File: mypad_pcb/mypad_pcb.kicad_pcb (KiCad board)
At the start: 2 copper layers, 76.2 x 96 mm, 59 parts, among them J1 USB_C_Receptacle_USB2.0, SW1 SW_BOOTMODE, SW10 +, SW11 4, SW12 5, SW13 6, SW14 1, SW15 2, SW16 3, SW17 0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

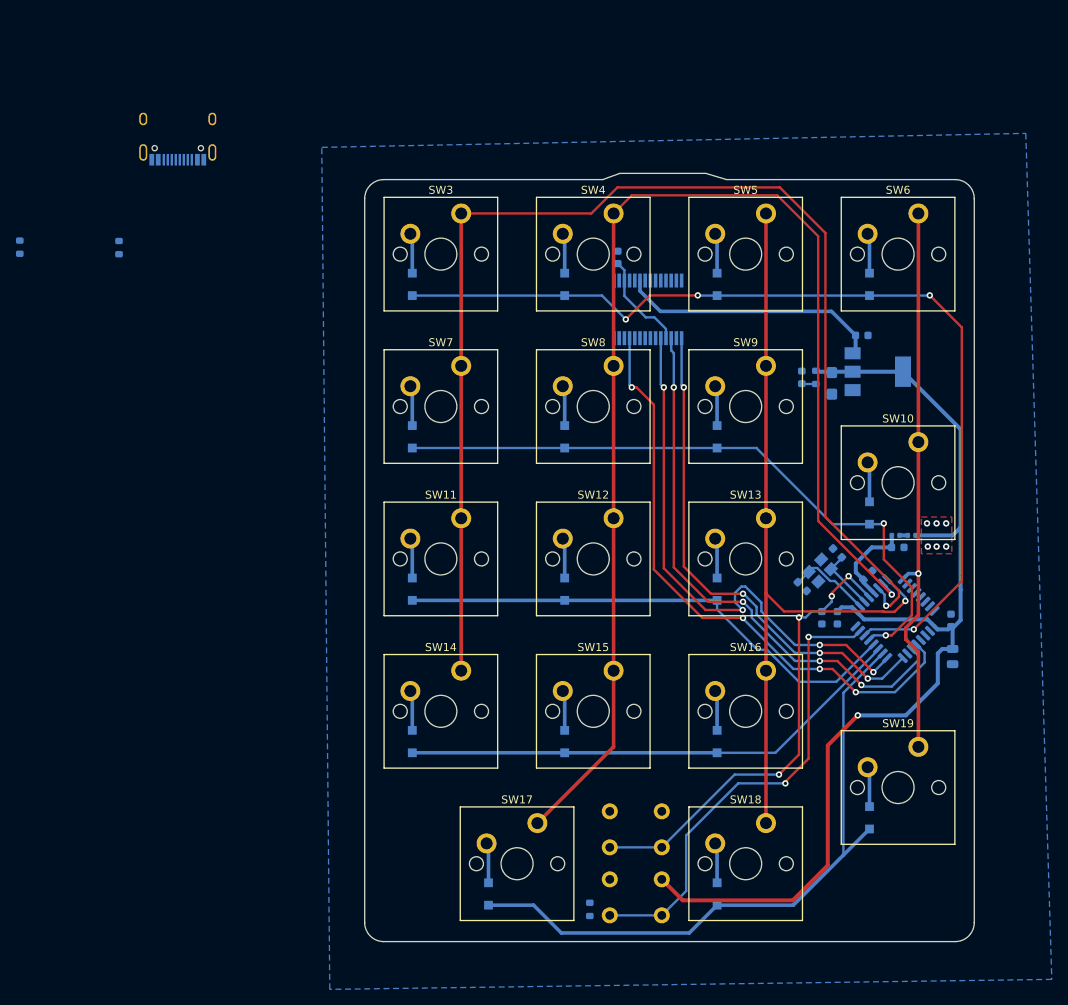
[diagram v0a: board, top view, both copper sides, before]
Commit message: Swap components for STM32F042C6 compatible ones
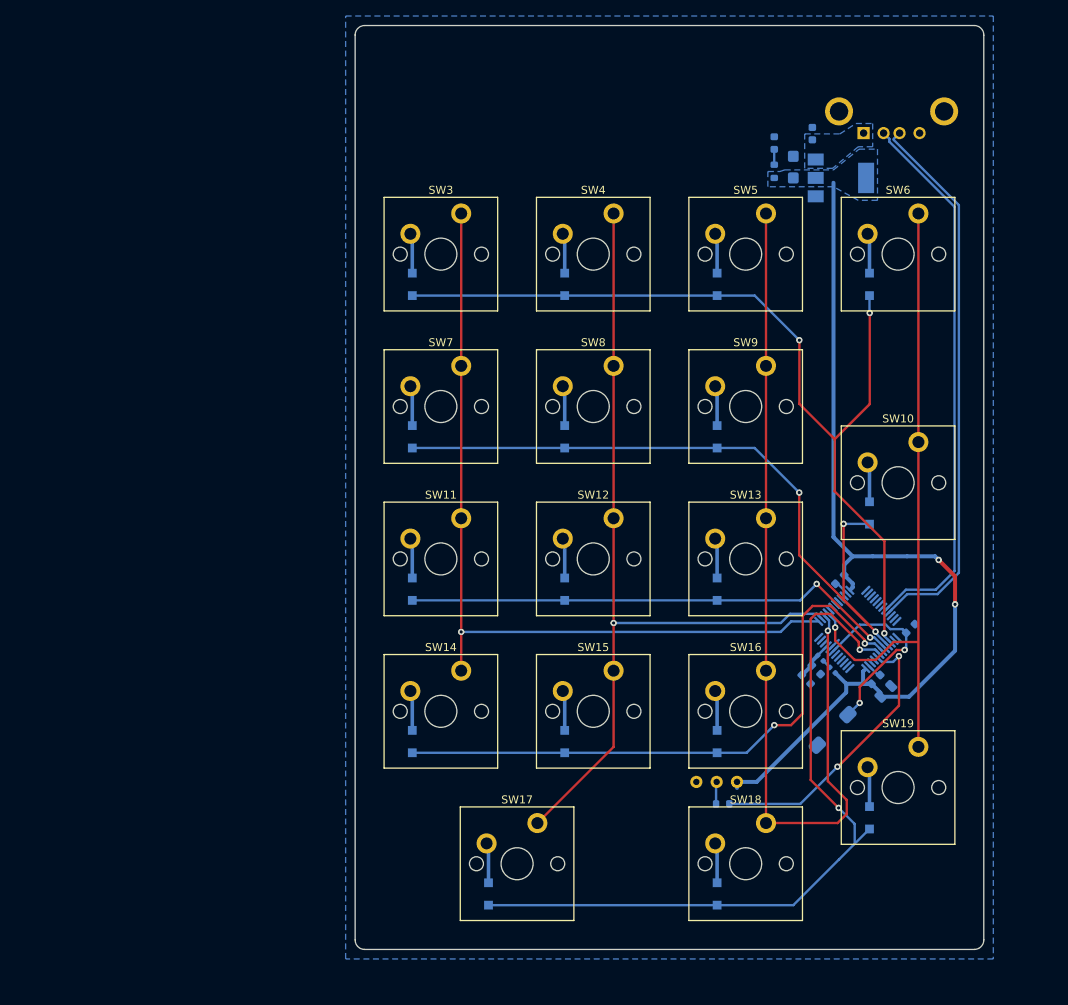
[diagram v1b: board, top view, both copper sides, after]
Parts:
- removed C1: 100n, Capacitor_SMD:C_0603_1608Metric
- removed C10, C11: 12p, Capacitor_SMD:C_0603_1608Metric
- removed R1, R2: 5k1, Resistor_SMD:R_0603_1608Metric
- removed U3: STM32F030K6Tx, Package_QFP:LQFP-32_7x7mm_P0.8mm
- removed Y1: 16MHz, Crystal:Crystal_SMD_3225-4Pin_3.2x2.5mm
- C9: value 0u1 -> 100n
- J1: value USB_C_Receptacle_USB2.0 -> USB_A; footprint Connector_USB:USB_C_Receptacle_HRO_TYPE-C-31-M-12 -> Connector_USB:USB_A_CONNFLY_DS1095-WNR0
- SW1: value SW_BOOTMODE -> SW_SPDT; footprint Button_Switch_THT:SW_PUSH_6mm -> Button_Switch_THT:ESP_SPDT_Slide_Switch
- SW2: footprint Button_Switch_THT:SW_PUSH_6mm -> Button_Switch_SMD:DTSM31N_SMD_Tact_Switch_4.3mm
- U1: value FT232RL -> STM32F042C6Tx; footprint Package_SO:SSOP-28_5.3x10.2mm_P0.65mm -> Package_QFP:LQFP-48_7x7mm_P0.5mm
- moved J1 85.7 mm to (175.5, 28.7)
- moved U1 47.8 mm to (174.8, 90.8), turned to 45 degrees
- moved D1 29.5 mm to (164.3, 30.0)
- moved C6 27.5 mm to (166.7, 33.0), turned to 90 degrees
- moved R4 26.3 mm to (164.3, 33.5), turned to 90 degrees
- moved C5 26.0 mm to (169.1, 28.8), turned to 90 degrees
- moved U2 24.7 mm to (172.6, 34.3)
- moved SW2 23.7 mm to (171.6, 103.3), turned to 45 degrees
- moved SW1 21.4 mm to (157.1, 109.8), turned to 90 degrees
- moved R3 21.2 mm to (157.9, 112.6), turned to 180 degrees
- moved L1 19.5 mm to (171.6, 95.8), turned to 135 degrees
- moved C8 18.4 mm to (169.5, 95.8), turned to -45 degrees
- moved L2 18.0 mm to (170.1, 94.3), turned to 135 degrees
- moved C7 15.1 mm to (168.3, 97.0), turned to -45 degrees
- moved C4 14.8 mm to (172.5, 84.5), turned to -135 degrees
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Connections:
- R3 pad 2: Earth -> Net-(R3-Pad2)
- SW1 pad 1: BOOT0 -> +3.3V
- SW1 pad 2: +3.3V -> Net-(R3-Pad2)
- U1 pad 1: USART_TX -> unconnected-(U1-Pad1)
- U1 pad 11: USART_CTS -> unconnected-(U1-Pad11)
- U1 pad 13: unconnected-(U1-Pad13) -> C1
- U1 pad 14: unconnected-(U1-Pad14) -> C2
- U1 pad 15: USBD+ -> C3
- U1 pad 16: USBD- -> C4
- U1 pad 17: /VCCIO -> unconnected-(U1-Pad17)
- U1 pad 18: Earth -> unconnected-(U1-Pad18)
- U1 pad 20: +5V -> unconnected-(U1-Pad20)
- U1 pad 21: Earth -> unconnected-(U1-Pad21)
- U1 pad 23: unconnected-(U1-Pad23) -> Earth
- U1 pad 24: (no net) -> +3.3V
- U1 pad 25: Earth -> unconnected-(U1-Pad25)
- U1 pad 26: Earth -> unconnected-(U1-Pad26)
- U1 pad 3: USART_RTS -> unconnected-(U1-Pad3)
- U1 pad 4: /VCCIO -> unconnected-(U1-Pad4)
- U1 pad 5: USART_RX -> unconnected-(U1-Pad5)
- U1 pad 7: Earth -> NRST
- U1 pad 8: (no net) -> Earth
- U1 pad 9: unconnected-(U1-Pad9) -> +3.3VA
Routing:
- net USART_CTS: track 75.0 -> 0.00 mm, vias 4 -> 0
- net USBD_P: track 0.00 -> 69.5 mm
- net USART_RTS: track 69.1 -> 0.00 mm, vias 4 -> 0
- net USBD_N: track 0.00 -> 69.0 mm
- net USART_RX: track 68.7 -> 0.00 mm, vias 4 -> 0
- net USART_TX: track 63.5 -> 0.00 mm, vias 4 -> 0
- net C1: track 160.4 -> 102.4 mm
- net C2: track 159.2 -> 106.9 mm
- net NRST: track 58.3 -> 25.0 mm, vias 4 -> 2
- net +5V: track 32.9 -> 0.00 mm
- net BOOT0: track 59.1 -> 35.8 mm
- net +3.3V: track 132.6 -> 117.3 mm, vias 1 -> 2
- net C3: track 98.8 -> 112.8 mm
- net R4: track 63.7 -> 76.2 mm, vias 0 -> 2
- net /VCCIO: track 12.5 -> 0.00 mm
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- added copper zone on B.Cu, net +3.3V
- added copper zone on B.Cu, net +5V
- removed copper zone on F.Cu, net Earth
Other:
- board size 76.2 x 96 mm -> 78.6 x 115.5 mm
